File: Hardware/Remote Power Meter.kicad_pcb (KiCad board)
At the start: 2 copper layers, 110 x 45 mm, 32 parts, among them J1 USB_C_Receptacle_USB2.0, J2 USB_A, J3 Conn_01x04_Male, J4 Conn_01x04_Female, J5 Conn_01x02, J6 Conn_01x02, SW1 SW_Push, U1 AMS1117-3.3, U2 INA219AxD, U3 CH340C

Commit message: Moved hardware into subfolder
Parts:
- moved R12 9.80 mm to (113.0, 85.2)
- moved SW1 7.20 mm to (121.1, 76.9), turned to -90 degrees
- moved R8 1.00 mm to (113.0, 91.0)
- moved R9 1.00 mm to (113.0, 94.0)
- renumbered J4 to J2, J5 to J4, J2 to J5
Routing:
- net RST: track 16.3 -> 22.6 mm
- net Net-(R9-Pad1): track 13.9 -> 14.9 mm
- net Net-(JP2-Pad2): track 19.2 -> 18.2 mm
- net Net-(R8-Pad1): track 10.5 -> 11.5 mm
- net Net-(JP1-Pad2): track 9.10 -> 8.10 mm

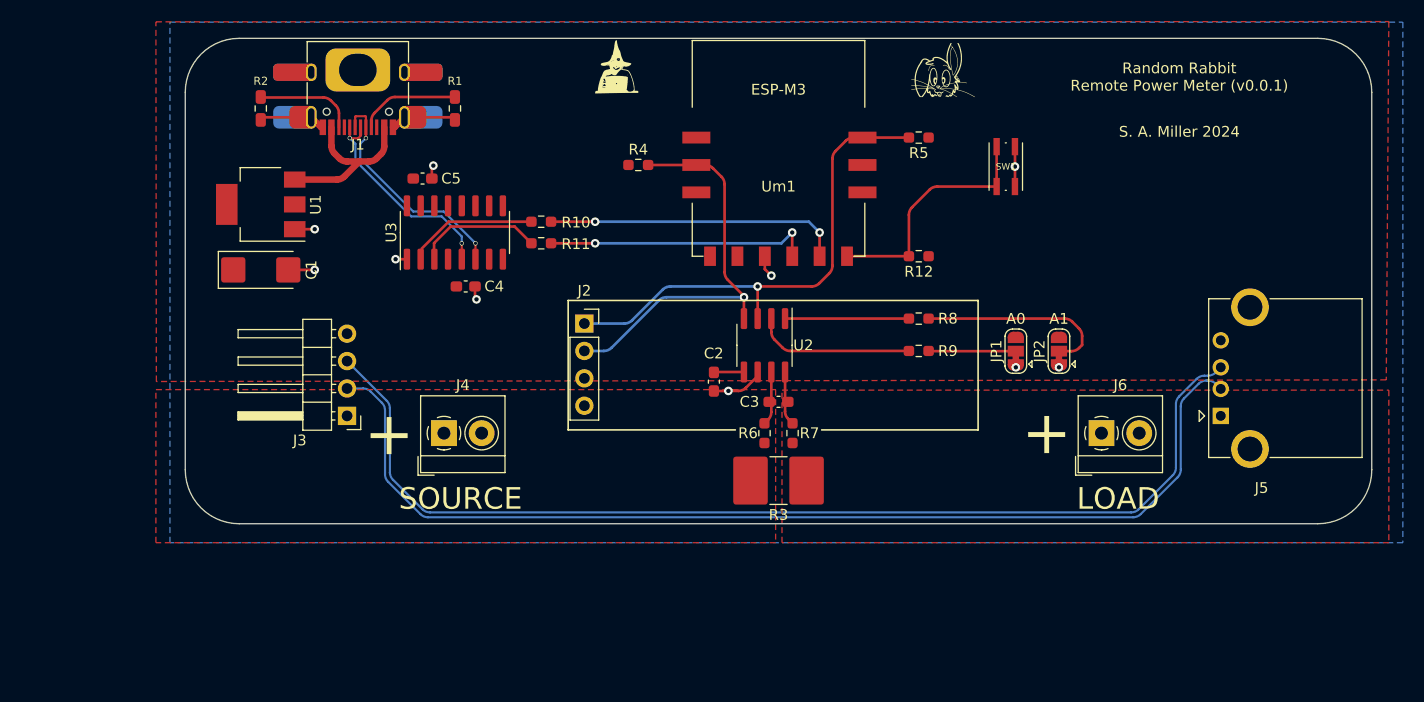
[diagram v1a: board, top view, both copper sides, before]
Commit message: Now programmable via USB
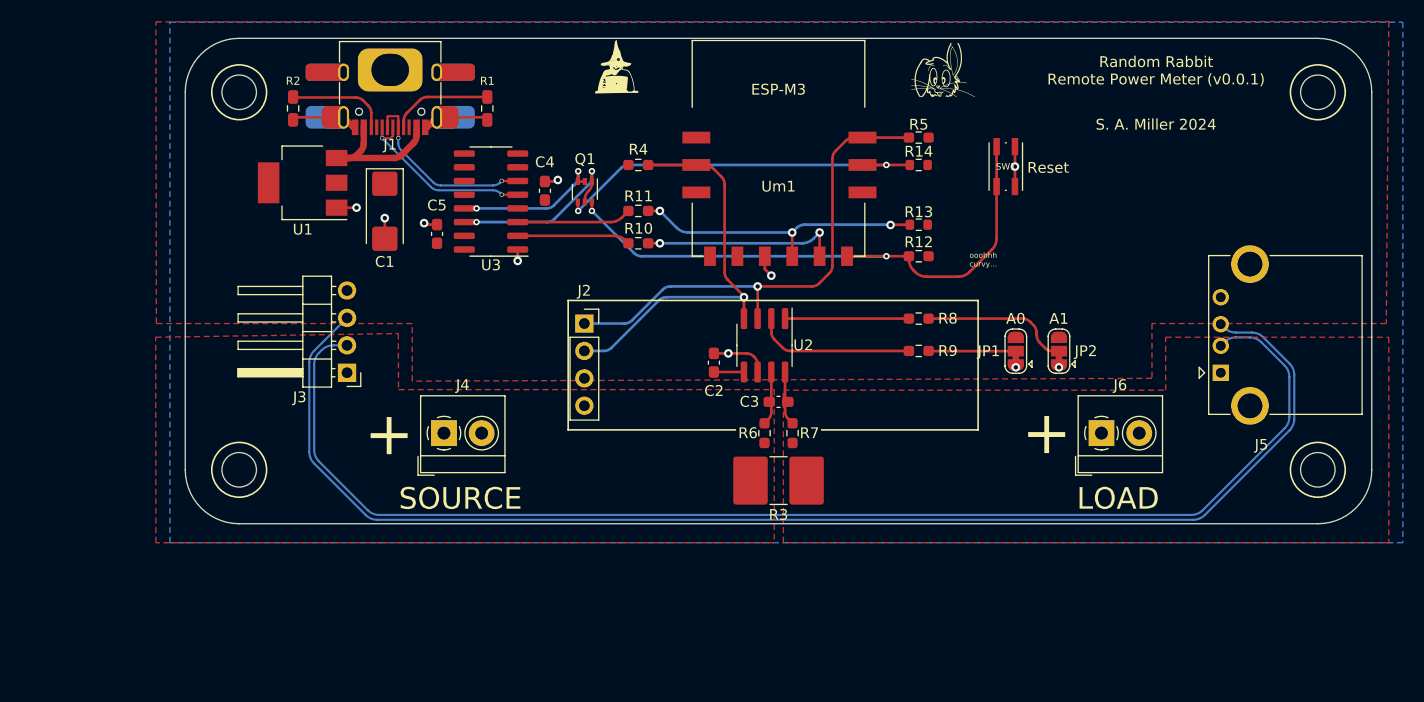
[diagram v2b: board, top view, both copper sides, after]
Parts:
- added Q1: UMH3N, Package_TO_SOT_SMD:SOT-363_SC-70-6, F.Cu at (82.0, 79.2)
- added R13: 10K, Resistor_SMD:R_0603_1608Metric, F.Cu at (113.0, 82.3)
- added R14: 10K, Resistor_SMD:R_0603_1608Metric, F.Cu at (113.0, 76.7)
- added REF**: Mount, Tinker:Mount, F.Cu at (150.0, 105.0)
- added REF**: Mount, Tinker:Mount, F.Cu at (150.0, 70.0)
- added REF**: Mount, Tinker:Mount, F.Cu at (50.0, 70.0)
- added REF**: Mount, Tinker:Mount, F.Cu at (50.0, 105.0)
- moved C1 12.7 mm to (63.5, 81.0), turned to -90 degrees
- moved C4 11.5 mm to (78.3, 79.1), turned to 90 degrees
- moved R11 9.49 mm to (87.0, 81.0)
- moved R10 9.22 mm to (87.0, 84.0)
- moved C5 5.30 mm to (68.3, 83.1), turned to 90 degrees
- moved U3 4.41 mm to (73.3, 80.1), turned to 180 degrees
- moved U1 4.37 mm to (55.9, 78.4)
- moved J3 4.00 mm to (60.0, 96.0)
- moved J5 4.00 mm to (141.0, 96.0)
- moved J1 3.00 mm to (64.0, 69.2)
- moved R1 3.00 mm to (73.0, 71.5)
- moved R2 3.00 mm to (55.0, 71.5)
- moved C2 1.76 mm to (94.0, 95.1), turned to 90 degrees
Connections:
- Um1 pad 1: unconnected-(Um1-Pad1) -> IO16
- Um1 pad 10: unconnected-(Um1-Pad10) -> IO2
- Um1 pad 11: unconnected-(Um1-Pad11) -> IO0
- Um1 pad 3: unconnected-(Um1-Pad3) -> IO13
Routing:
- net IO0: track 0.00 -> 35.5 mm, vias 0 -> 2
- net RST: track 22.6 -> 55.0 mm, vias 0 -> 2
- net D+: track 99.9 -> 125.0 mm
- net D-: track 99.0 -> 121.1 mm
- net RTS: track 0.00 -> 16.1 mm, vias 0 -> 2
- net DTR: track 0.00 -> 12.9 mm, vias 0 -> 2
- net RxD: track 27.5 -> 18.4 mm
- net Net-(JP2-Pad2): track 18.2 -> 13.8 mm
- net UD-: track 21.5 -> 17.4 mm
- net Vcc: track 16.5 -> 13.9 mm
- net UD+: track 20.1 -> 17.5 mm
- net TxD: track 25.0 -> 27.5 mm, vias 2 -> 3
- net Net-(R11-Pad1): track 11.8 -> 10.6 mm
- net Net-(R10-Pad1): track 11.2 -> 10.5 mm
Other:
- board text added: "Reset"
- board text added: "ooohhh curvy..."

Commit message: Possibly reached v1.0.0
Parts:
- added C6: 0.1, Capacitor_SMD:C_0603_1608Metric_Pad1.08x0.95mm_HandSolder, F.Cu at (70.0, 90.2)
- added C7: 0.1, Capacitor_SMD:C_0603_1608Metric_Pad1.08x0.95mm_HandSolder, F.Cu at (130.0, 91.8)
- added D1: WS2812B, LED_SMD:LED_WS2812B_PLCC4_5.0x5.0mm_P3.2mm, F.Cu at (75.0, 91.0)
- added D2: WS2812B, LED_SMD:LED_WS2812B_PLCC4_5.0x5.0mm_P3.2mm, F.Cu at (125.0, 91.0)
- added J7: Conn_01x04_Male, Connector_PinHeader_2.54mm:PinHeader_1x04_P2.54mm_Vertical, F.Cu at (135.0, 96.0)
- added R15: 470, Resistor_SMD:R_0603_1608Metric_Pad0.98x0.95mm_HandSolder, F.Cu at (82.3, 86.3)
- added USB1: 48037-0001, Tinker:USB-A-TH_48037-0001, F.Cu at (48.8, 92.2)
- J3: footprint Connector_PinHeader_2.54mm:PinHeader_1x04_P2.54mm_Horizontal -> Connector_PinHeader_2.54mm:PinHeader_1x04_P2.54mm_Vertical
- moved JP1 10.3 mm to (111.8, 93.5)
- moved JP2 9.63 mm to (116.4, 93.5)
- moved R8 7.34 mm to (105.7, 90.5)
- moved R9 7.34 mm to (105.7, 93.5)
- moved J3 5.00 mm to (65.0, 96.0)
- moved J4 4.45 mm to (65.0, 103.6)
- moved J6 2.54 mm to (131.5, 103.6)
- moved G*** 0.62 mm to (85.0, 68.2)
- moved REF** 0.38 mm to (115.0, 68.2)
- moved J5 0.31 mm to (141.0, 95.7)
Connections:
- net /Vload renamed Vload
- net /Vsource renamed Vsource
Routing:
- net Net-(D1-Pad2): track 0.00 -> 59.1 mm, vias 0 -> 2
- net D-: track 121.1 -> 149.0 mm
- net D+: track 125.0 -> 152.0 mm
- net IO13: track 0.00 -> 14.0 mm
- net GND: track 29.3 -> 37.9 mm, vias 10 -> 13
- net Net-(R9-Pad1): track 14.9 -> 7.72 mm
- net Net-(R8-Pad1): track 11.5 -> 4.33 mm
- net Net-(D1-Pad4): track 0.00 -> 6.05 mm
- net Net-(JP1-Pad2): track 8.10 -> 5.18 mm
- net Net-(JP2-Pad2): track 13.8 -> 11.5 mm
- net RST: track 55.0 -> 55.8 mm
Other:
- board text added: "Alerts"
- board text added: "Connection"
- board text added: "G"

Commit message: ...
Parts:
- added JP3: vLED, Jumper:SolderJumper-3_P1.3mm_Bridged12_RoundedPad1.0x1.5mm, F.Cu at (130.9, 85.7)
- added R16: 10K, Resistor_SMD:R_0603_1608Metric_Pad0.98x0.95mm_HandSolder, F.Cu at (87.0, 99.0)
- added R2: 0.1, Resistor_SMD:R_2816_7142Metric_Pad3.20x4.45mm_HandSolder, F.Cu at (100.0, 119.5)
- moved C6 48.4 mm to (118.3, 86.7), turned to 0 degrees
- moved D1 44.9 mm to (119.9, 90.5)
- moved R15 31.1 mm to (113.0, 91.3), turned to 0 degrees
- moved SW1 17.0 mm to (130.9, 90.8), turned to 0 degrees
- moved D2 16.0 mm to (141.0, 90.5)
- moved REF** 13.9 mm to (145.0, 118.0)
- moved REF** 13.9 mm to (55.0, 118.0)
- moved C4 13.0 mm to (78.3, 92.1)
- moved J2 13.0 mm to (53.8, 104.2)
- moved J3 13.0 mm to (70.0, 108.0)
- moved J4 13.0 mm to (70.0, 115.6)
- moved J5 13.0 mm to (136.0, 107.7)
- moved J6 13.0 mm to (126.5, 115.6)
- moved J7 13.0 mm to (130.0, 108.0)
- moved R8 13.0 mm to (60.0, 83.5)
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- renumbered J2 to Disp1, USB1 to J2, R3 to R1, R4 to R10, R10 to R12, R12 to R17, R6 to R3, R7 to R4, R9 to R5, R8 to R6, R1 to R7, R2 to R8, R5 to R9
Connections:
- C6 pad 1: 3v3 -> Net-(C6-Pad1)
- C7 pad 1: 3v3 -> Net-(C6-Pad1)
- D1 pad 1: 3v3 -> Net-(C6-Pad1)
- D2 pad 1: 3v3 -> Net-(C6-Pad1)
- R15 pad 1: IO13 -> IO0
- Um1 pad 4: unconnected-(Um1-Pad4) -> /EN
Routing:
- net Vcc: track 13.9 -> 77.7 mm, vias 0 -> 2
- net D+: track 152.0 -> 91.1 mm
- net D-: track 149.0 -> 91.1 mm
- net Net-(D1-Pad2): track 59.1 -> 28.9 mm, vias 2 -> 0
- net Net-(C6-Pad1): track 0.00 -> 29.9 mm
- net IO13: track 14.0 -> 0.00 mm
- net Vsource: track 0.00 -> 9.56 mm
- net Vload: track 0.00 -> 9.56 mm
- net RST: track 55.8 -> 62.3 mm
- net /EN: track 0.00 -> 6.39 mm
- net IO0: track 35.5 -> 39.4 mm
- net Net-(D1-Pad4): track 6.05 -> 9.28 mm
- net UD+: track 17.5 -> 14.6 mm
- net UD-: track 17.4 -> 15.0 mm
- net I2C SCL: track 37.9 -> 35.7 mm
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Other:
- board size 110 x 45 mm -> 100 x 46 mm
- board text added: "(LED voltage)"
- board text added: "3v3"
- board text added: "5v0"
- board text removed: "ooohhh curvy..."

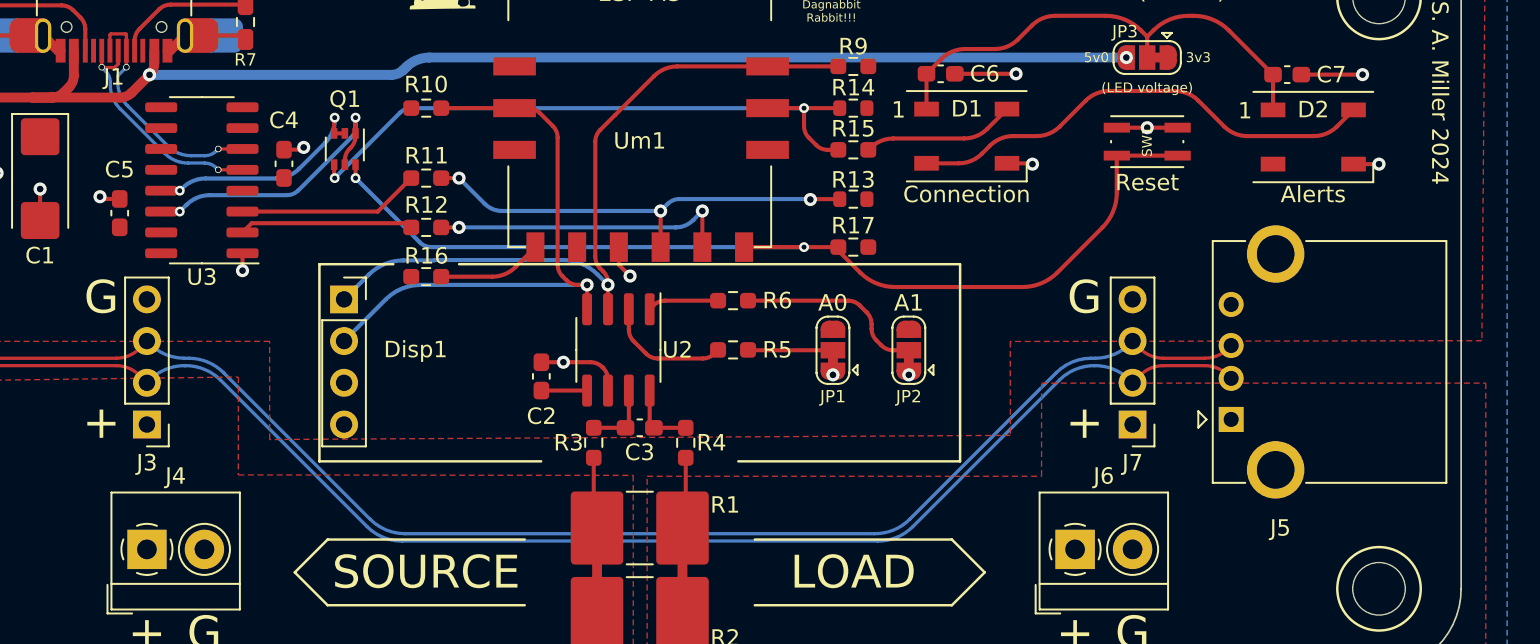
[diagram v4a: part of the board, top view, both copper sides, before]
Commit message: Added LCSC BOM
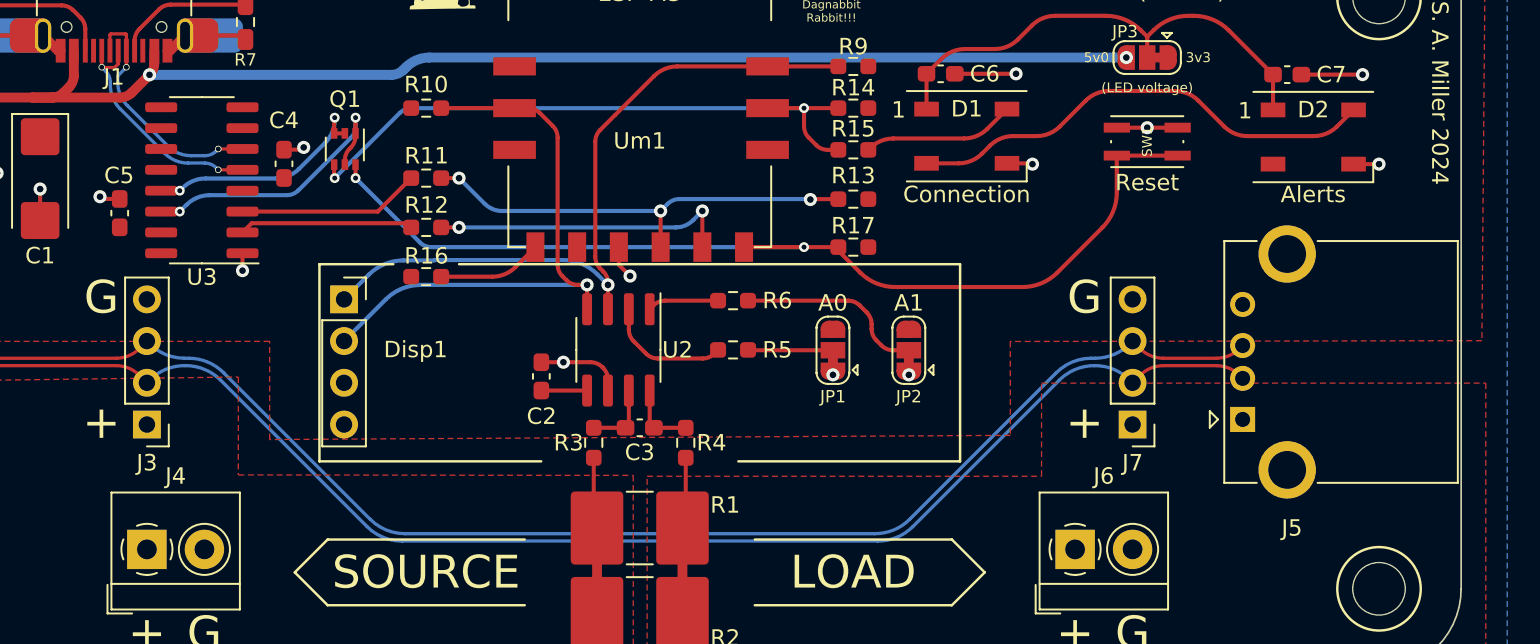
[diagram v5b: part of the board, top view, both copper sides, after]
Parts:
- C5: value 100nf -> 0.1
- Disp1: value Conn_01x04_Female -> Cheap Ali OLED
- R13, R14: footprint Resistor_SMD:R_0603_1608Metric -> Resistor_SMD:R_0603_1608Metric_Pad0.98x0.95mm_HandSolder
- U2: value INA219AxD -> INA219
- moved J5 0.70 mm to (136.7, 107.7)
- turned C5 to -90 degrees
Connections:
- C5 pad 1: 3v3 -> GND
- C5 pad 2: GND -> 3v3
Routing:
- net D-: track 91.1 -> 91.8 mm
- net D+: track 91.1 -> 91.8 mm
